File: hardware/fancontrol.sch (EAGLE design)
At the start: 0 parts

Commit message: fan control
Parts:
- added C1: 470u, rcl:CPOL-EUE5-10.5
- added Q1: IRLZ44Z, transistor-power:IRLZ44Z
- added R1, R2, R3: 10k, rcl:R-EU_0207/7
- added T1: BC547, transistor:BC547
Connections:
- new net +12V: Q1.D, R3.1
- new net FAN+: C1.+, Q1.S
- new net GND: C1.-, T1.E
- new net N$1: R1.2, T1.B
- new net N$2: R2.1, T1.C
- new net N$3: Q1.G, R2.2, R3.2
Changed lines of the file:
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@@
 <parts>
 <part name="FRAME1" library="frames" deviceset="DINA4_L" device=""/>
+<part name="P+1" library="supply1" deviceset="+5V" device=""/>
+<part name="P+2" library="supply1" deviceset="+12V" device=""/>
+<part name="GND1" library="supply1" deviceset="GND" device=""/>
+<part name="Q1" library="transistor-power" deviceset="IRLZ44Z" device=""/>
+<part name="R1" library="rcl" deviceset="R-EU_" device="0207/7" value="10k"/>
+<part name="T1" library="transistor" deviceset="BC547" device=""/>
+<part name="R2" library="rcl" deviceset="R-EU_" device="0207/7" value="10k"/>
+<part name="R3" library="rcl" deviceset="R-EU_" device="0207/7" value="10k"/>
+<part name="C1" library="rcl" deviceset="CPOL-EU" device="E5-10.5" value="470u"/>
+<part name="GND2" library="supply1" deviceset="GND" device=""/>
 </parts>
 <sheets>
@@
 <instance part="FRAME1" gate="G$1" x="0" y="0"/>
 <instance part="FRAME1" gate="G$2" x="162.56" y="0"/>
+<instance part="P+1" gate="1" x="55.88" y="99.06"/>
+<instance part="P+2" gate="1" x="78.74" y="109.22"/>
+<instance part="GND1" gate="1" x="104.14" y="66.04"/>
+<instance part="Q1" gate="G$1" x="101.6" y="101.6" rot="R90"/>
+<instance part="R1" gate="G$1" x="91.44" y="76.2"/>
+<instance part="T1" gate="G$1" x="101.6" y="76.2"/>
+<instance part="R2" gate="G$1" x="104.14" y="88.9" rot="R90"/>
+<instance part="R3" gate="G$1" x="91.44" y="96.52"/>
+<instance part="C1" gate="G$1" x="116.84" y="99.06"/>
+<instance part="GND2" gate="1" x="116.84" y="66.04"/>
 </instances>
 <busses>
 </busses>
 <nets>
+<net name="N$1" class="0">
+<segment>
+<pinref part="R1" gate="G$1" pin="2"/>
+<pinref part="T1" gate="G$1" pin="B"/>
+<wire x1="96.52" y1="76.2" x2="99.06" y2="76.2" width="0.1524" layer="91"/>
+</segment>
+</net>
+<net name="N$2" class="0">
+<segment>
+<pinref part="R2" gate="G$1" pin="1"/>
+<pinref part="T1" gate="G$1" pin="C"/>
+<wire x1="104.14" y1="83.82" x2="104.14" y2="81.28" width="0.1524" layer="91"/>
+</segment>
+</net>
+<net name="GND" class="0">
+<segment>
+<pinref part="T1" gate="G$1" pin="E"/>
+<pinref part="GND1" gate="1" pin="GND"/>
+<wire x1="104.14" y1="71.12" x2="104.14" y2="68.58" width="0.1524" layer="91"/>
+</segment>
+<segment>
+<pinref part="C1" gate="G$1" pin="-"/>
+<pinref part="GND2" gate="1" pin="GND"/>
+<wire x1="116.84" y1="93.98" x2="116.84" y2="68.58" width="0.1524" layer="91"/>
+</segment>
+</net>
+<net name="N$3" class="0">
+<segment>
+<pinref part="R2" gate="G$1" pin="2"/>
+<pinref part="Q1" gate="G$1" pin="G"/>
+<wire x1="104.14" y1="93.98" x2="104.14" y2="96.52" width="0.1524" layer="91"/>
+<pinref part="R3" gate="G$1" pin="2"/>
+<wire x1="104.14" y1="96.52" x2="104.14" y2="99.06" width="0.1524" layer="91"/>
+<wire x1="96.52" y1="96.52" x2="104.14" y2="96.52" width="0.1524" layer="91"/>
+<junction x="104.14" y="96.52"/>
+</segment>
+</net>
+<net name="+12V" class="0">
+<segment>
+<pinref part="Q1" gate="G$1" pin="D"/>
+<pinref part="P+2" gate="1" pin="+12V"/>
+<wire x1="96.52" y1="104.14" x2="78.74" y2="104.14" width="0.1524" layer="91"/>
+<wire x1="78.74" y1="104.14" x2="78.74" y2="106.68" width="0.1524" layer="91"/>
+<pinref part="R3" gate="G$1" pin="1"/>
+<wire x1="86.36" y1="96.52" x2="78.74" y2="96.52" width="0.1524" layer="91"/>
+<wire x1="78.74" y1="96.52" x2="78.74" y2="104.14" width="0.1524" layer="91"/>
+<junction x="78.74" y="104.14"/>
+</segment>
+</net>
+<net name="FAN+" class="0">
+<segment>
+<pinref part="Q1" gate="G$1" pin="S"/>
+<pinref part="C1" gate="G$1" pin="+"/>
+<wire x1="106.68" y1="104.14" x2="116.84" y2="104.14" width="0.1524" layer="91"/>
+<wire x1="116.84" y1="104.14" x2="116.84" y2="101.6" width="0.1524" layer="91"/>
+<wire x1="116.84" y1="104.14" x2="127" y2="104.14" width="0.1524" layer="91"/>
+<junction x="116.84" y="104.14"/>
+<label x="127" y="104.14" size="1.27" layer="95" xref="yes"/>
+</segment>
+</net>
 </nets>
 </sheet>

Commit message: ad
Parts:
- added ARDUINO1: ARDUINO, arduino:ARDUINO
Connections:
- new net +5V: ARDUINO1.5V
- net +12V: now also ARDUINO1.VIN
- net GND: now also ARDUINO1.GND
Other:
- moved on the sheet: C1, Q1, R1, R2, R3, T1
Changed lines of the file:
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@@
 <parts>
 <part name="FRAME1" library="frames" deviceset="DINA4_L" device=""/>
-<part name="P+1" library="supply1" deviceset="+5V" device=""/>
 <part name="P+2" library="supply1" deviceset="+12V" device=""/>
 <part name="GND1" library="supply1" deviceset="GND" device=""/>
@@
 <part name="C1" library="rcl" deviceset="CPOL-EU" device="E5-10.5" value="470u"/>
 <part name="GND2" library="supply1" deviceset="GND" device=""/>
+<part name="ARDUINO1" library="arduino" deviceset="ARDUINO" device=""/>
+<part name="GND3" library="supply1" deviceset="GND" device=""/>
+<part name="P+3" library="supply1" deviceset="+12V" device=""/>
+<part name="P+4" library="supply1" deviceset="+5V" device=""/>
 </parts>
 <sheets>
@@
 <instance part="FRAME1" gate="G$1" x="0" y="0"/>
 <instance part="FRAME1" gate="G$2" x="162.56" y="0"/>
-<instance part="P+1" gate="1" x="55.88" y="99.06"/>
-<instance part="P+2" gate="1" x="78.74" y="109.22"/>
-<instance part="GND1" gate="1" x="104.14" y="66.04"/>
-<instance part="Q1" gate="G$1" x="101.6" y="101.6" rot="R90"/>
-<instance part="R1" gate="G$1" x="91.44" y="76.2"/>
-<instance part="T1" gate="G$1" x="101.6" y="76.2"/>
-<instance part="R2" gate="G$1" x="104.14" y="88.9" rot="R90"/>
-<instance part="R3" gate="G$1" x="91.44" y="96.52"/>
-<instance part="C1" gate="G$1" x="116.84" y="99.06"/>
-<instance part="GND2" gate="1" x="116.84" y="66.04"/>
+<instance part="P+2" gate="1" x="111.76" y="137.16"/>
+<instance part="GND1" gate="1" x="137.16" y="93.98"/>
+<instance part="Q1" gate="G$1" x="134.62" y="129.54" rot="R90"/>
+<instance part="R1" gate="G$1" x="124.46" y="104.14"/>
+<instance part="T1" gate="G$1" x="134.62" y="104.14"/>
+<instance part="R2" gate="G$1" x="137.16" y="116.84" rot="R90"/>
+<instance part="R3" gate="G$1" x="124.46" y="124.46"/>
+<instance part="C1" gate="G$1" x="149.86" y="127"/>
+<instance part="GND2" gate="1" x="149.86" y="93.98"/>
+<instance part="ARDUINO1" gate="G$1" x="50.8" y="50.8"/>
+<instance part="GND3" gate="1" x="10.16" y="53.34"/>
+<instance part="P+3" gate="1" x="5.08" y="91.44"/>
+<instance part="P+4" gate="1" x="12.7" y="91.44"/>
 </instances>
 <busses>
@@
 <pinref part="R1" gate="G$1" pin="2"/>
 <pinref part="T1" gate="G$1" pin="B"/>
-<wire x1="96.52" y1="76.2" x2="99.06" y2="76.2" width="0.1524" layer="91"/>
+<wire x1="129.54" y1="104.14" x2="132.08" y2="104.14" width="0.1524" layer="91"/>
 </segment>
 </net>
@@
 <pinref part="R2" gate="G$1" pin="1"/>
 <pinref part="T1" gate="G$1" pin="C"/>
-<wire x1="104.14" y1="83.82" x2="104.14" y2="81.28" width="0.1524" layer="91"/>
+<wire x1="137.16" y1="111.76" x2="137.16" y2="109.22" width="0.1524" layer="91"/>
 </segment>
 </net>
@@
 <pinref part="T1" gate="G$1" pin="E"/>
 <pinref part="GND1" gate="1" pin="GND"/>
-<wire x1="104.14" y1="71.12" x2="104.14" y2="68.58" width="0.1524" layer="91"/>
+<wire x1="137.16" y1="99.06" x2="137.16" y2="96.52" width="0.1524" layer="91"/>
 </segment>
 <segment>
 <pinref part="C1" gate="G$1" pin="-"/>
 <pinref part="GND2" gate="1" pin="GND"/>
-<wire x1="116.84" y1="93.98" x2="116.84" y2="68.58" width="0.1524" layer="91"/>
+<wire x1="149.86" y1="121.92" x2="149.86" y2="96.52" width="0.1524" layer="91"/>
+</segment>
+<segment>
+<pinref part="ARDUINO1" gate="G$1" pin="GND"/>
+<pinref part="GND3" gate="1" pin="GND"/>
+<wire x1="25.4" y1="66.04" x2="10.16" y2="66.04" width="0.1524" layer="91"/>
+<wire x1="10.16" y1="66.04" x2="10.16" y2="55.88" width="0.1524" layer="91"/>
 </segment>
 </net>
@@
 <pinref part="R2" gate="G$1" pin="2"/>
 <pinref part="Q1" gate="G$1" pin="G"/>
-<wire x1="104.14" y1="93.98" x2="104.14" y2="96.52" width="0.1524" layer="91"/>
+<wire x1="137.16" y1="121.92" x2="137.16" y2="124.46" width="0.1524" layer="91"/>
 <pinref part="R3" gate="G$1" pin="2"/>
-<wire x1="104.14" y1="96.52" x2="104.14" y2="99.06" width="0.1524" layer="91"/>
-<wire x1="96.52" y1="96.52" x2="104.14" y2="96.52" width="0.1524" layer="91"/>
-<junction x="104.14" y="96.52"/>
+<wire x1="137.16" y1="124.46" x2="137.16" y2="127" width="0.1524" layer="91"/>
+<wire x1="129.54" y1="124.46" x2="137.16" y2="124.46" width="0.1524" layer="91"/>
+<junction x="137.16" y="124.46"/>
 </segment>
 </net>
@@
 <pinref part="Q1" gate="G$1" pin="D"/>
 <pinref part="P+2" gate="1" pin="+12V"/>
-<wire x1="96.52" y1="104.14" x2="78.74" y2="104.14" width="0.1524" layer="91"/>
-<wire x1="78.74" y1="104.14" x2="78.74" y2="106.68" width="0.1524" layer="91"/>
+<wire x1="129.54" y1="132.08" x2="111.76" y2="132.08" width="0.1524" layer="91"/>
+<wire x1="111.76" y1="132.08" x2="111.76" y2="134.62" width="0.1524" layer="91"/>
 <pinref part="R3" gate="G$1" pin="1"/>
-<wire x1="86.36" y1="96.52" x2="78.74" y2="96.52" width="0.1524" layer="91"/>
-<wire x1="78.74" y1="96.52" x2="78.74" y2="104.14" width="0.1524" layer="91"/>
-<junction x="78.74" y="104.14"/>
+<wire x1="119.38" y1="124.46" x2="111.76" y2="124.46" width="0.1524" layer="91"/>
+<wire x1="111.76" y1="124.46" x2="111.76" y2="132.08" width="0.1524" layer="91"/>
+<junction x="111.76" y="132.08"/>
+</segment>
+<segment>
+<pinref part="ARDUINO1" gate="G$1" pin="VIN"/>
+<pinref part="P+3" gate="1" pin="+12V"/>
+<wire x1="25.4" y1="60.96" x2="5.08" y2="60.96" width="0.1524" layer="91"/>
+<wire x1="5.08" y1="60.96" x2="5.08" y2="88.9" width="0.1524" layer="91"/>
 </segment>
 </net>
@@
 <pinref part="Q1" gate="G$1" pin="S"/>
 <pinref part="C1" gate="G$1" pin="+"/>
-<wire x1="106.68" y1="104.14" x2="116.84" y2="104.14" width="0.1524" layer="91"/>
-<wire x1="116.84" y1="104.14" x2="116.84" y2="101.6" width="0.1524" layer="91"/>
-<wire x1="116.84" y1="104.14" x2="127" y2="104.14" width="0.1524" layer="91"/>
-<junction x="116.84" y="104.14"/>
-<label x="127" y="104.14" size="1.27" layer="95" xref="yes"/>
+<wire x1="139.7" y1="132.08" x2="149.86" y2="132.08" width="0.1524" layer="91"/>
+<wire x1="149.86" y1="132.08" x2="149.86" y2="129.54" width="0.1524" layer="91"/>
+<wire x1="149.86" y1="132.08" x2="160.02" y2="132.08" width="0.1524" layer="91"/>
+<junction x="149.86" y="132.08"/>
+<label x="160.02" y="132.08" size="1.27" layer="95" xref="yes"/>
 </segment>
 </net>
+<net name="+5V" class="0">
+<segment>
+<pinref part="ARDUINO1" gate="G$1" pin="5V"/>
+<pinref part="P+4" gate="1" pin="+5V"/>
+<wire x1="25.4" y1="71.12" x2="12.7" y2="71.12" width="0.1524" layer="91"/>
+<wire x1="12.7" y1="71.12" x2="12.7" y2="88.9" width="0.1524" layer="91"/>
+</segment>
+</net>

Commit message: generated board
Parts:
- added JP1: (no value), pinhead:PINHD-1X3
- added R4: 4k7, rcl:R-EU_0207/7
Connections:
- new net DQ: JP1.2, R4.2
- net +12V: no longer ARDUINO1.VIN
- net +5V: now also JP1.3, R4.1
- net GND: now also JP1.1
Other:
- note added: "to DS18S20"
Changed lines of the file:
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@@
 <part name="ARDUINO1" library="arduino" deviceset="ARDUINO" device=""/>
 <part name="GND3" library="supply1" deviceset="GND" device=""/>
-<part name="P+3" library="supply1" deviceset="+12V" device=""/>
 <part name="P+4" library="supply1" deviceset="+5V" device=""/>
+<part name="JP1" library="pinhead" deviceset="PINHD-1X3" device=""/>
+<part name="P+1" library="supply1" deviceset="+5V" device=""/>
+<part name="GND4" library="supply1" deviceset="GND" device=""/>
+<part name="R4" library="rcl" deviceset="R-EU_" device="0207/7" value="4k7"/>
 </parts>
 <sheets>
 <sheet>
 <plain>
+<text x="40.64" y="142.24" size="1.27" layer="91" rot="R90">to DS18S20</text>
 </plain>
 <instances>
@@
 <instance part="ARDUINO1" gate="G$1" x="50.8" y="50.8"/>
 <instance part="GND3" gate="1" x="10.16" y="53.34"/>
-<instance part="P+3" gate="1" x="5.08" y="91.44"/>
 <instance part="P+4" gate="1" x="12.7" y="91.44"/>
+<instance part="JP1" gate="A" x="43.18" y="147.32" rot="R180"/>
+<instance part="P+1" gate="1" x="55.88" y="160.02"/>
+<instance part="GND4" gate="1" x="55.88" y="134.62"/>
+<instance part="R4" gate="G$1" x="63.5" y="149.86" smashed="yes">
+<attribute name="NAME" x="59.69" y="151.3586" size="1.778" layer="95"/>
+<attribute name="VALUE" x="64.77" y="151.638" size="1.778" layer="96"/>
+</instance>
 </instances>
 <busses>
@@
 <wire x1="10.16" y1="66.04" x2="10.16" y2="55.88" width="0.1524" layer="91"/>
 </segment>
+<segment>
+<pinref part="JP1" gate="A" pin="1"/>
+<pinref part="GND4" gate="1" pin="GND"/>
+<wire x1="45.72" y1="144.78" x2="55.88" y2="144.78" width="0.1524" layer="91"/>
+<wire x1="55.88" y1="144.78" x2="55.88" y2="137.16" width="0.1524" layer="91"/>
+</segment>
 </net>
 <net name="N$3" class="0">
@@
 <junction x="111.76" y="132.08"/>
 </segment>
-<segment>
-<pinref part="ARDUINO1" gate="G$1" pin="VIN"/>
-<pinref part="P+3" gate="1" pin="+12V"/>
-<wire x1="25.4" y1="60.96" x2="5.08" y2="60.96" width="0.1524" layer="91"/>
-<wire x1="5.08" y1="60.96" x2="5.08" y2="88.9" width="0.1524" layer="91"/>
-</segment>
 </net>
 <net name="FAN+" class="0">
@@
 <wire x1="12.7" y1="71.12" x2="12.7" y2="88.9" width="0.1524" layer="91"/>
 </segment>
+<segment>
+<pinref part="JP1" gate="A" pin="3"/>
+<pinref part="R4" gate="G$1" pin="1"/>
+<wire x1="45.72" y1="149.86" x2="55.88" y2="149.86" width="0.1524" layer="91"/>
+<pinref part="P+1" gate="1" pin="+5V"/>
+<wire x1="55.88" y1="149.86" x2="58.42" y2="149.86" width="0.1524" layer="91"/>
+<wire x1="55.88" y1="157.48" x2="55.88" y2="149.86" width="0.1524" layer="91"/>
+<junction x="55.88" y="149.86"/>
+</segment>
 </net>
+<net name="DQ" class="0">
+<segment>
+<pinref part="JP1" gate="A" pin="2"/>
+<wire x1="45.72" y1="147.32" x2="71.12" y2="147.32" width="0.1524" layer="91"/>
+<label x="73.66" y="147.32" size="1.27" layer="95" xref="yes"/>
+<wire x1="71.12" y1="147.32" x2="73.66" y2="147.32" width="0.1524" layer="91"/>
+<wire x1="71.12" y1="149.86" x2="71.12" y2="147.32" width="0.1524" layer="91"/>
+<junction x="71.12" y="147.32"/>
+<pinref part="R4" gate="G$1" pin="2"/>
+<wire x1="68.58" y1="149.86" x2="71.12" y2="149.86" width="0.1524" layer="91"/>
+</segment>
+</net>

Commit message: populated the pcb
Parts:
- added JP2: (no value), pinhead:PINHD-1X3
- added R5: 10k, rcl:R-EU_0207/7
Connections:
- new net N$5: JP2.3
- new net PWM: ARDUINO1.PWM_05, R1.1
- new net TACHO: ARDUINO1.PWM_03, JP2.2, R5.1
- net +12V: now also ARDUINO1.VIN
- net +5V: now also R5.2
- net DQ: now also ARDUINO1.04
- net FAN+: now also JP2.1
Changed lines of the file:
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@@
 <part name="GND4" library="supply1" deviceset="GND" device=""/>
 <part name="R4" library="rcl" deviceset="R-EU_" device="0207/7" value="4k7"/>
+<part name="P+3" library="supply1" deviceset="+12V" device=""/>
+<part name="JP2" library="pinhead" deviceset="PINHD-1X3" device=""/>
+<part name="GND5" library="supply1" deviceset="GND" device=""/>
+<part name="R5" library="rcl" deviceset="R-EU_" device="0207/7" value="10k"/>
+<part name="P+5" library="supply1" deviceset="+5V" device=""/>
 </parts>
 <sheets>
@@
 <attribute name="VALUE" x="64.77" y="151.638" size="1.778" layer="96"/>
 </instance>
+<instance part="P+3" gate="1" x="5.08" y="91.44"/>
+<instance part="JP2" gate="A" x="218.44" y="111.76"/>
+<instance part="GND5" gate="1" x="200.66" y="101.6"/>
+<instance part="R5" gate="G$1" x="200.66" y="119.38" rot="R90"/>
+<instance part="P+5" gate="1" x="200.66" y="129.54"/>
 </instances>
 <busses>
@@
 <junction x="111.76" y="132.08"/>
 </segment>
+<segment>
+<pinref part="ARDUINO1" gate="G$1" pin="VIN"/>
+<pinref part="P+3" gate="1" pin="+12V"/>
+<wire x1="25.4" y1="60.96" x2="5.08" y2="60.96" width="0.1524" layer="91"/>
+<wire x1="5.08" y1="60.96" x2="5.08" y2="88.9" width="0.1524" layer="91"/>
+</segment>
 </net>
 <net name="FAN+" class="0">
@@
 <label x="160.02" y="132.08" size="1.27" layer="95" xref="yes"/>
 </segment>
+<segment>
+<pinref part="JP2" gate="A" pin="1"/>
+<wire x1="215.9" y1="114.3" x2="210.82" y2="114.3" width="0.1524" layer="91"/>
+<label x="210.82" y="114.3" size="1.27" layer="95" rot="R180" xref="yes"/>
+</segment>
 </net>
 <net name="+5V" class="0">
@@
 <wire x1="55.88" y1="157.48" x2="55.88" y2="149.86" width="0.1524" layer="91"/>
 <junction x="55.88" y="149.86"/>
+</segment>
+<segment>
+<pinref part="P+5" gate="1" pin="+5V"/>
+<pinref part="R5" gate="G$1" pin="2"/>
+<wire x1="200.66" y1="127" x2="200.66" y2="124.46" width="0.1524" layer="91"/>
 </segment>
 </net>
@@
 <wire x1="68.58" y1="149.86" x2="71.12" y2="149.86" width="0.1524" layer="91"/>
 </segment>
-</net>
+<segment>
+<pinref part="ARDUINO1" gate="G$1" pin="04"/>
+<wire x1="76.2" y1="35.56" x2="81.28" y2="35.56" width="0.1524" layer="91"/>
+<label x="81.28" y="35.56" size="1.27" layer="95" xref="yes"/>
+</segment>
+</net>
+<net name="TACHO" class="0">
+<segment>
+<pinref part="ARDUINO1" gate="G$1" pin="PWM_03"/>
+<wire x1="76.2" y1="30.48" x2="81.28" y2="30.48" width="0.1524" layer="91"/>
+<label x="81.28" y="30.48" size="1.27" layer="95" xref="yes"/>
+</segment>
+<segment>
+<pinref part="JP2" gate="A" pin="2"/>
+<wire x1="215.9" y1="111.76" x2="200.66" y2="111.76" width="0.1524" layer="91"/>
+<pinref part="R5" gate="G$1" pin="1"/>
+<wire x1="200.66" y1="114.3" x2="200.66" y2="111.76" width="0.1524" layer="91"/>
+<wire x1="200.66" y1="111.76" x2="198.12" y2="111.76" width="0.1524" layer="91"/>
+<junction x="200.66" y="111.76"/>
+<label x="198.12" y="111.76" size="1.27" layer="95" rot="R180" xref="yes"/>
+</segment>
+</net>
+<net name="PWM" class="0">
+<segment>
+<pinref part="ARDUINO1" gate="G$1" pin="PWM_05"/>
+<wire x1="76.2" y1="40.64" x2="81.28" y2="40.64" width="0.1524" layer="91"/>
+<label x="81.28" y="40.64" size="1.27" layer="95" xref="yes"/>
+</segment>
+<segment>
+<pinref part="R1" gate="G$1" pin="1"/>
+<wire x1="119.38" y1="104.14" x2="116.84" y2="104.14" width="0.1524" layer="91"/>
+<label x="116.84" y="104.14" size="1.27" layer="95" rot="R180" xref="yes"/>
+</segment>
+</net>
+<net name="N$5" class="0">
+<segment>
+<pinref part="JP2" gate="A" pin="3"/>
+<wire x1="215.9" y1="109.22" x2="200.66" y2="109.22" width="0.1524" layer="91"/>
+<wire x1="200.66" y1="109.22" x2="200.66" y2="104.14" width="0.1524" layer="91"/>
+<pinref part="GND5" gate="1" pin="GND"/>
+</segment>
+</net>

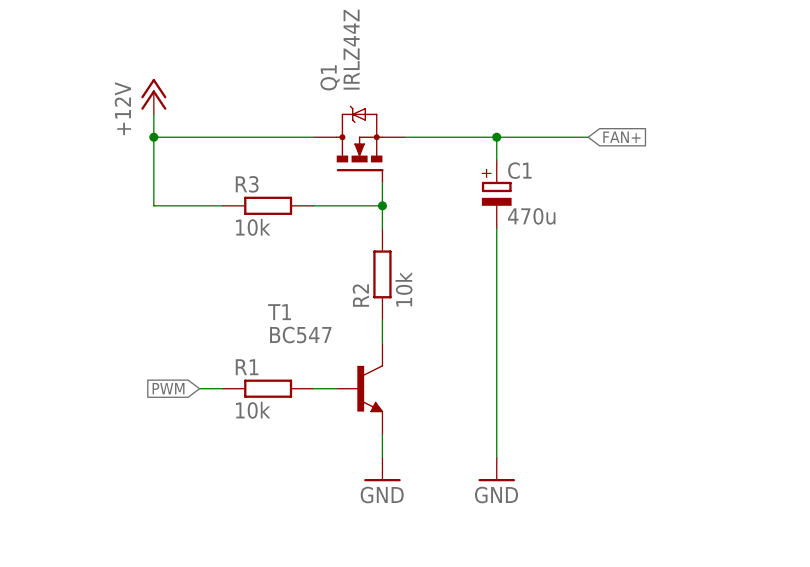
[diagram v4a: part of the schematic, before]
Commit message: changed R2 from 10k to 10R
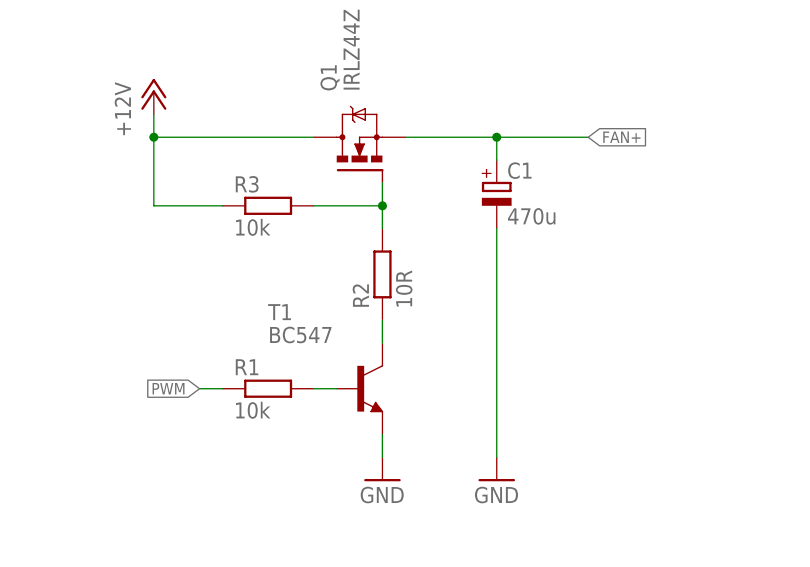
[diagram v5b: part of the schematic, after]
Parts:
- R2: value 10k -> 10R
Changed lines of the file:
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@@
 <part name="R1" library="rcl" deviceset="R-EU_" device="0207/7" value="10k"/>
 <part name="T1" library="transistor" deviceset="BC547" device=""/>
-<part name="R2" library="rcl" deviceset="R-EU_" device="0207/7" value="10k"/>
+<part name="R2" library="rcl" deviceset="R-EU_" device="0207/7" value="10R"/>
 <part name="R3" library="rcl" deviceset="R-EU_" device="0207/7" value="10k"/>
 <part name="C1" library="rcl" deviceset="CPOL-EU" device="E5-10.5" value="470u"/>

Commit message: connect JP2 to GND. Fixes #2
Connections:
- removed net N$5: JP2.3
- net GND: now also JP2.3
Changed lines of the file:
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@@
 <?xml version="1.0" encoding="utf-8"?>
 <!DOCTYPE eagle SYSTEM "eagle.dtd">
-<eagle version="6.2">
+<eagle version="6.4">
 <drawing>
 <settings>
@@
 <wire x1="55.88" y1="144.78" x2="55.88" y2="137.16" width="0.1524" layer="91"/>
 </segment>
+<segment>
+<pinref part="JP2" gate="A" pin="3"/>
+<pinref part="GND5" gate="1" pin="GND"/>
+<wire x1="215.9" y1="109.22" x2="200.66" y2="109.22" width="0.1524" layer="91"/>
+<wire x1="200.66" y1="109.22" x2="200.66" y2="104.14" width="0.1524" layer="91"/>
+</segment>
 </net>
 <net name="N$3" class="0">
@@
 </segment>
 </net>
-<net name="N$5" class="0">
-<segment>
-<pinref part="JP2" gate="A" pin="3"/>
-<wire x1="215.9" y1="109.22" x2="200.66" y2="109.22" width="0.1524" layer="91"/>
-<wire x1="200.66" y1="109.22" x2="200.66" y2="104.14" width="0.1524" layer="91"/>
-<pinref part="GND5" gate="1" pin="GND"/>
-</segment>
-</net>
